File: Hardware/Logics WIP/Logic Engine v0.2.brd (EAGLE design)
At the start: 61 x 30.5 mm, 36 parts, among them IC1 MEGA328P, Y1 16MHz

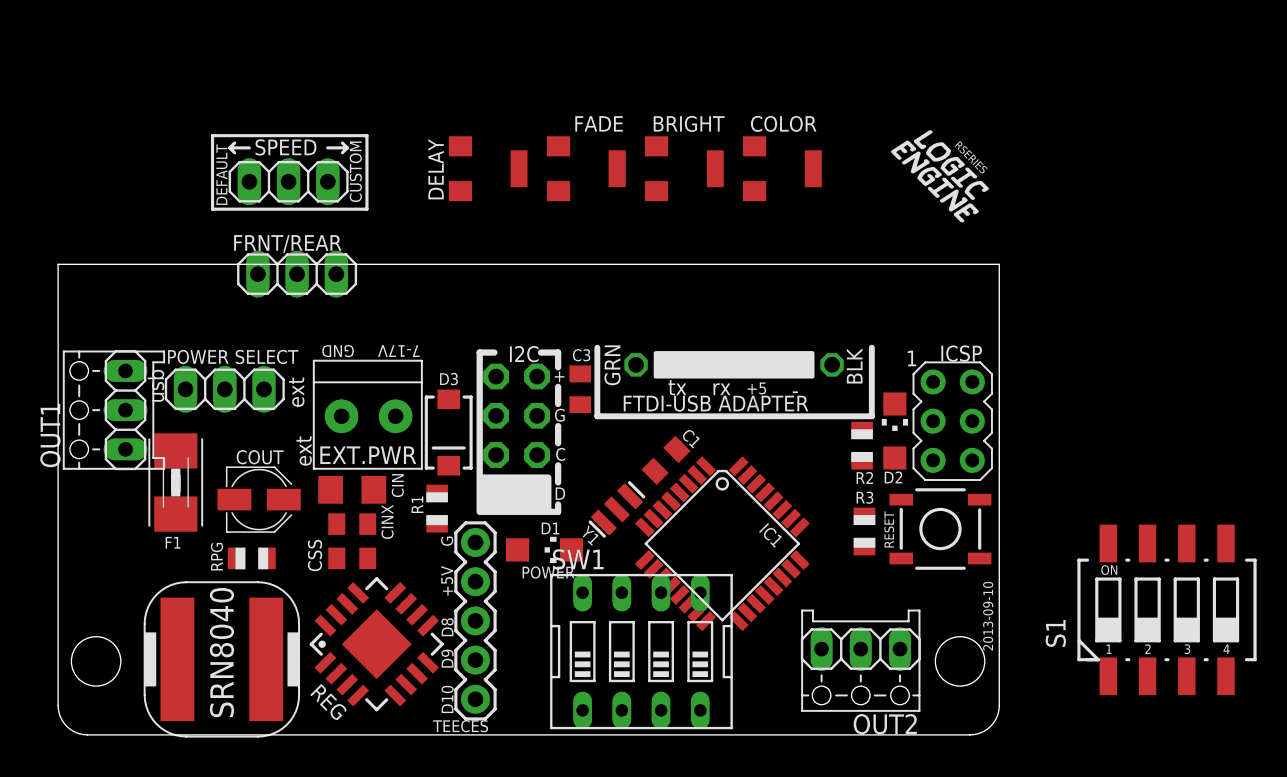
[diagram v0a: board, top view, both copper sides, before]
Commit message: added microSD card holder to the RSeries library and Logic Engine (still unfinished)
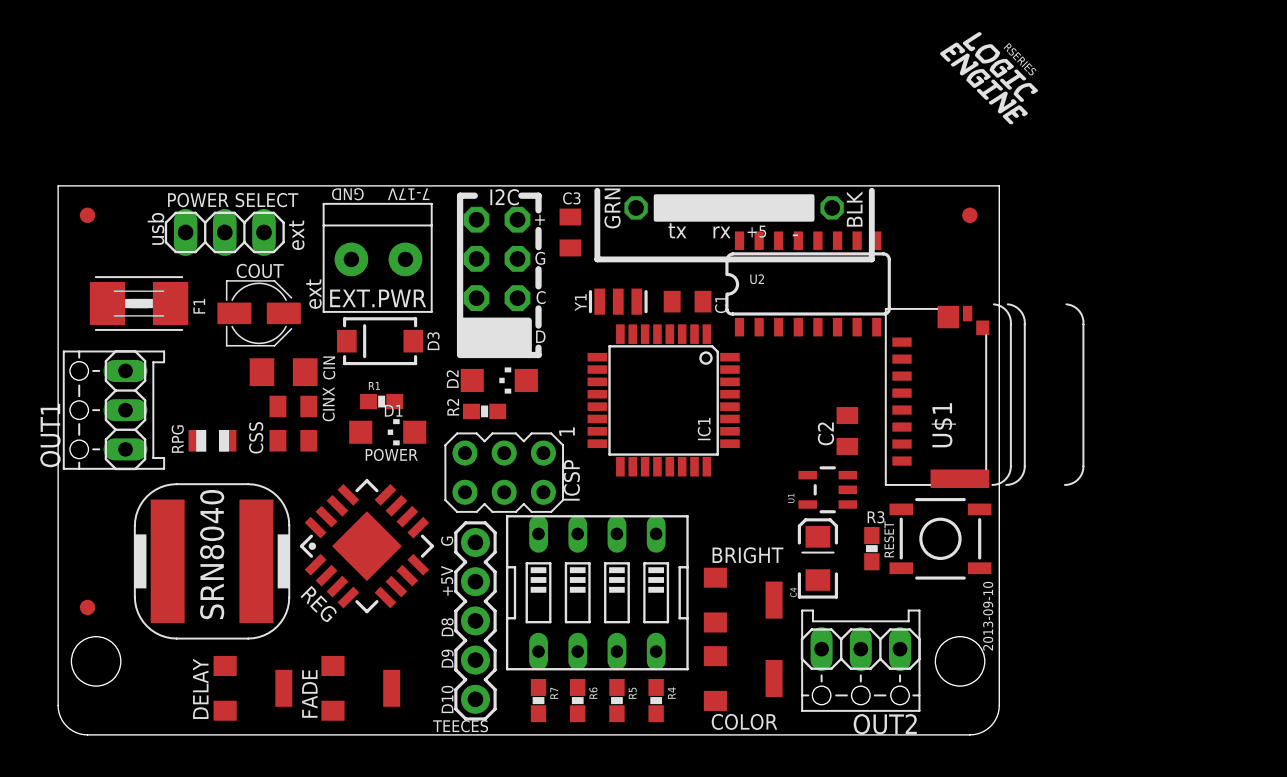
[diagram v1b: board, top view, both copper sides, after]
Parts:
- removed FRNT/REAR, SPEED: (no value), pinhead:1X03
- removed JP1: (no value), carduino:1X06-CLEAN
- removed S1: 219-04, switch-dil:CTS-219-04
- added C2: 0.1uF, adafruit:C0805K
- added C4: 10uF, SparkFun-Capacitors:EIA3216
- added FID1, FID2, FID3: FIDUCIAL1X2.5, SparkFun-Aesthetics:FIDUCIAL-1X2.5
- added FTDI: (no value), carduino:1X06-CLEAN
- added R4, R5, R6, R7: 10K, SparkFun-Resistors:0603-RES
- added U$1: MICROSD, rseries:MICROSD_SMALL
- added U1: V_REG_LDOSMD, SparkFun-PowerIC:SOT23-5
- added U2: HEX_CONVERTER, SparkFun-DigitalIC:SO016
- R1, R2: device adafruit:R0805 -> SparkFun-Resistors:0603-RES
- R3: value 10k -> 10K; device adafruit:R0805 -> SparkFun-Resistors:0603-RES
- moved DELAY 36.9 mm to (12.6, 3.02)
- moved FADE 36.7 mm to (19.6, 3.02)
- moved COLOR 33.1 mm to (44.4, 3.65)
- moved ICSP 29.2 mm to (28.9, 17.0), turned to 270 degrees
- moved BRIGHT 28.2 mm to (44.4, 8.73)
- moved D2 25.8 mm to (28.6, 23.0), turned to 270 degrees
- moved R2 24.5 mm to (27.6, 21.0), turned to 180 degrees
- moved Y1 13.5 mm to (36.3, 28.1), turned to 180 degrees
- moved D1 12.7 mm to (21.3, 19.6)
- moved COUT 12.1 mm to (13.0, 27.3)
- moved F1 11.8 mm to (5.24, 27.9), turned to 180 degrees
- moved C1 10.4 mm to (40.8, 28.1), turned to 0 degrees
- moved I2C 10.2 mm to (27.1, 29.6)
- moved I2C1 10.2 mm to (29.8, 29.6)
- moved C3 10.2 mm to (33.2, 32.5)
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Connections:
- new net N$12: R4.1, SW1.8
- new net N$13: R5.1, SW1.7
- new net N$14: R6.1, SW1.6
- new net N$15: R7.1, SW1.5
- new net N$16: U$1.3, U2.4
- new net N$17: U$1.5, U2.6
- new net N$18: U$1.2, U2.2
- new net N$19: C4.A, U1.5, U2.1
- net +5V: now also C2.1, R1.1, R3.1, U$1.4, U1.1, U1.3; no longer FRNT/REAR.1, R1.2, R3.2, SPEED.1
- net DIGITAL10: now also U2.3; no longer TEECES.5
- net DIGITAL2: now also SW1.1
- net DIGITAL3: now also SW1.2
- net DIGITAL4: now also SW1.3
- net DIGITAL5: now also SW1.4; no longer SPEED.2
- net DIGITAL7: now also TEECES.5; no longer FRNT/REAR.2
- net GND: now also C2.2, C4.C, FTDI.1, FTDI.2, R4.2, R5.2, R6.2, R7.2, U$1.6, U$1.MT1, U$1.MT2, U1.2, U2.8; no longer FRNT/REAR.3, JP1.1, JP1.2, SPEED.3
- net MISO: now also U$1.7
- net MOSI: now also U2.5
- net N$5: now also R1.2; no longer R1.1
- net RST: now also R3.2; no longer R3.1
- net RTS#: now also FTDI.6; no longer JP1.6
- net RXD: now also FTDI.4; no longer JP1.4
- net SCK: now also U2.7
- net TXD: now also FTDI.5; no longer JP1.5
- net USB_5V: now also FTDI.3; no longer JP1.3
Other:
- board size 61 x 30.5 mm -> 61 x 35.6 mm
- board text removed: "CUSTOM"
- board text removed: "DEFAULT"
- board text removed: "FTDI-USB ADAPTER"
